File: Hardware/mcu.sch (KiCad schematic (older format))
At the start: 30 parts, among them J1 SWD_programming, U6 CY8C4246AZI-L445, Y1 Crystal

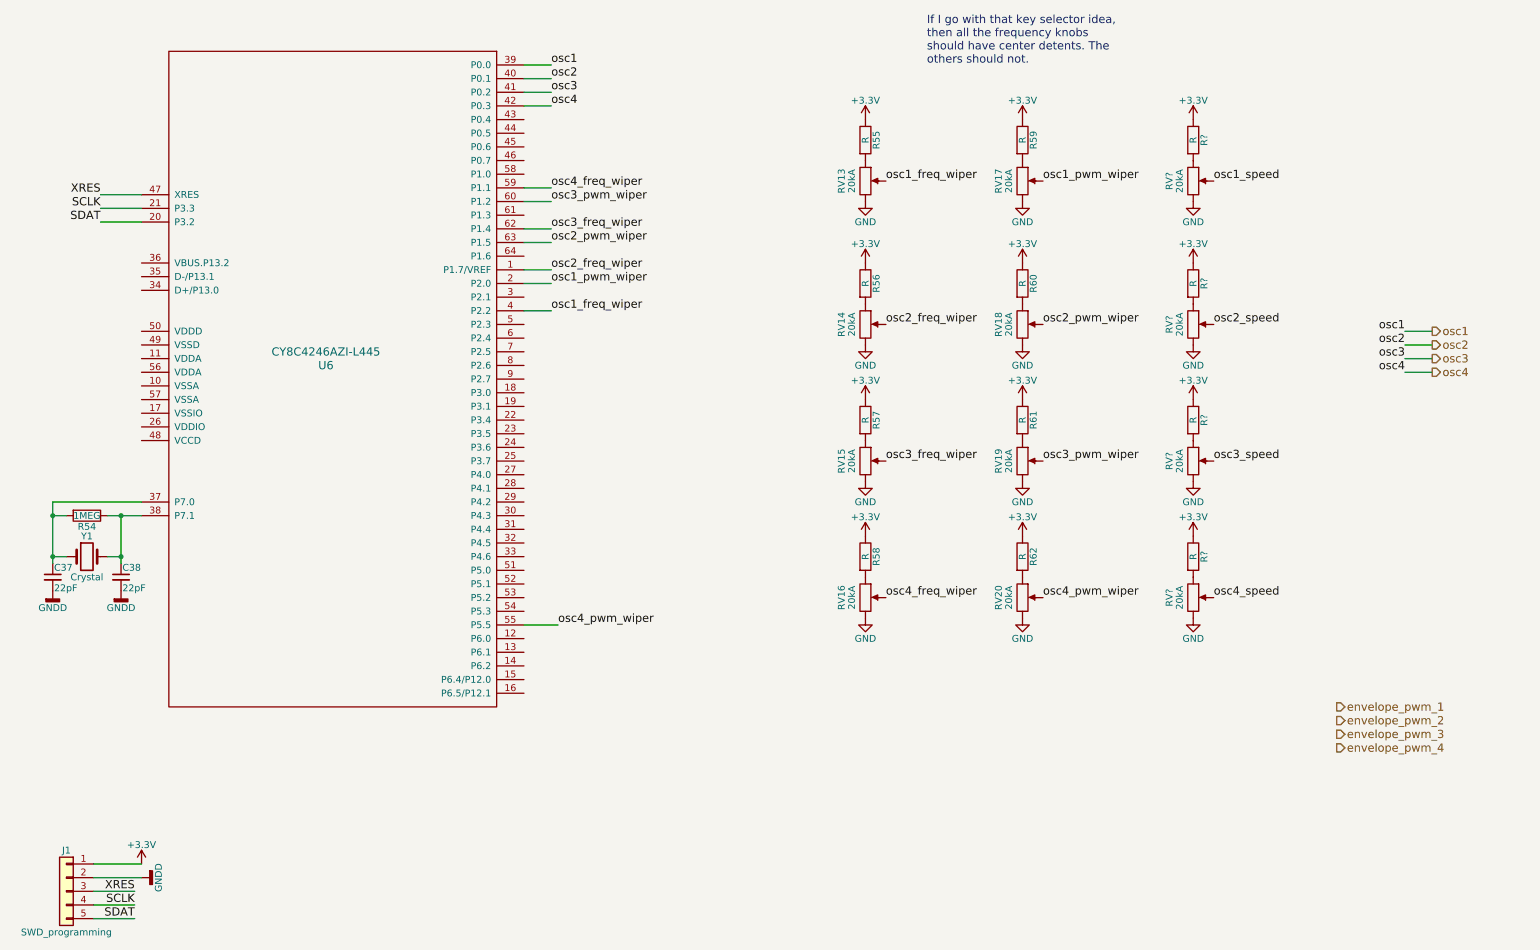
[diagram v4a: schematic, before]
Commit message: update pinout with latest changes for production IC
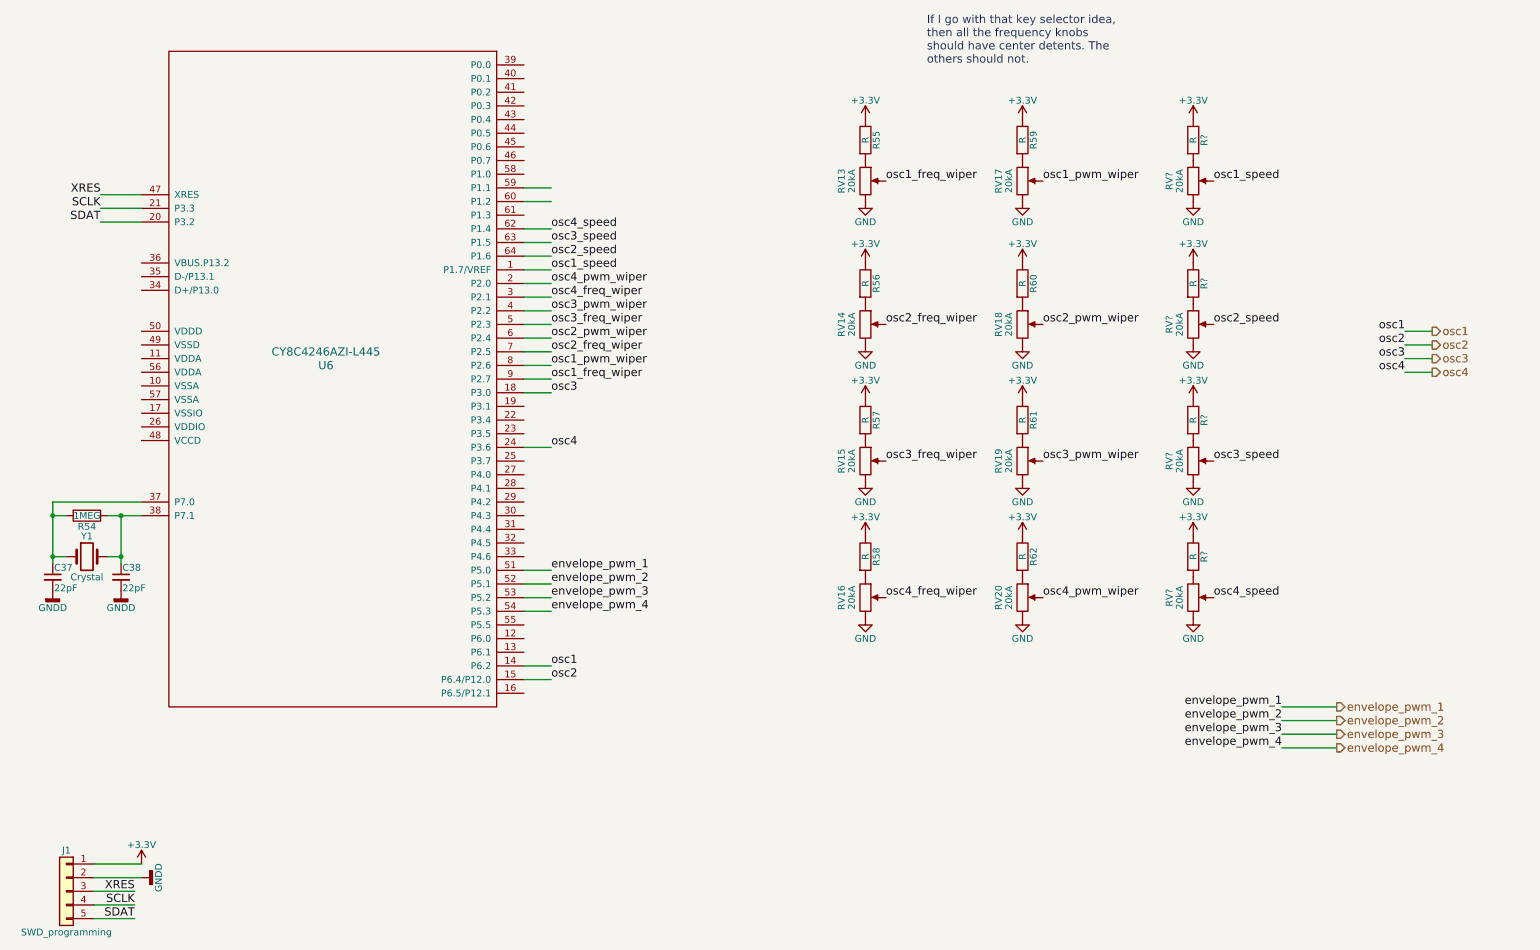
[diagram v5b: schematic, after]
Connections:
- wire segments 31 -> 45
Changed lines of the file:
@@
 	-1   0    0    -1
 $EndComp
+Text Label 4400 3400 0    60   ~ 0
+osc1_freq_wiper
+Wire Wire Line
+	4400 2900 4200 2900
+Text Label 4400 3300 0    60   ~ 0
+osc1_pwm_wiper
+Wire Wire Line
+	4400 2700 4200 2700
+Text Label 4400 3200 0    60   ~ 0
+osc2_freq_wiper
+Wire Wire Line
+	4400 2600 4200 2600
+Text Label 4400 3100 0    60   ~ 0
+osc2_pwm_wiper
+Wire Wire Line
+	4400 2400 4200 2400
+Text Label 4400 3000 0    60   ~ 0
+osc3_freq_wiper
+Wire Wire Line
+	4400 2300 4200 2300
 Text Label 4400 2900 0    60   ~ 0
-osc1_freq_wiper
-Wire Wire Line
-	4400 2900 4200 2900
+osc3_pwm_wiper
+Wire Wire Line
+	4400 2100 4200 2100
+Text Label 4400 2800 0    60   ~ 0
+osc4_freq_wiper
+Wire Wire Line
+	4400 2000 4200 2000
 Text Label 4400 2700 0    60   ~ 0
-osc1_pwm_wiper
-Wire Wire Line
-	4400 2700 4200 2700
-Text Label 4400 2600 0    60   ~ 0
-osc2_freq_wiper
-Wire Wire Line
-	4400 2600 4200 2600
-Text Label 4400 2400 0    60   ~ 0
-osc2_pwm_wiper
-Wire Wire Line
-	4400 2400 4200 2400
-Text Label 4400 2300 0    60   ~ 0
-osc3_freq_wiper
-Wire Wire Line
-	4400 2300 4200 2300
-Text Label 4400 2100 0    60   ~ 0
-osc3_pwm_wiper
-Wire Wire Line
-	4400 2100 4200 2100
-Text Label 4400 2000 0    60   ~ 0
-osc4_freq_wiper
-Wire Wire Line
-	4400 2000 4200 2000
-Text Label 4450 5200 0    60   ~ 0
 osc4_pwm_wiper
-Wire Wire Line
-	4450 5200 4200 5200
-Text Label 4400 1100 0    60   ~ 0
+Text Label 4400 5500 0    60   ~ 0
 osc1
-Text Label 4400 1200 0    60   ~ 0
+Text Label 4400 5600 0    60   ~ 0
 osc2
-Text Label 4400 1300 0    60   ~ 0
+Text Label 4400 3500 0    60   ~ 0
 osc3
-Text Label 4400 1400 0    60   ~ 0
+Text Label 4400 3900 0    60   ~ 0
 osc4
-Wire Wire Line
-	4400 1100 4200 1100
-Wire Wire Line
-	4400 1200 4200 1200
-Wire Wire Line
-	4200 1300 4400 1300
-Wire Wire Line
-	4400 1400 4200 1400
 Text Label 10650 3050 2    60   ~ 0
 osc1
@@
 	1    0    0    -1
 $EndComp
+Wire Wire Line
+	4400 3400 4200 3400
+Wire Wire Line
+	4400 3300 4200 3300
+Wire Wire Line
+	4400 3200 4200 3200
+Wire Wire Line
+	4400 3100 4200 3100
+Wire Wire Line
+	4400 3000 4200 3000
+Wire Wire Line
+	4400 2800 4200 2800
+Text Label 4400 2600 0    60   ~ 0
+osc1_speed
+Text Label 4400 2500 0    60   ~ 0
+osc2_speed
+Text Label 4400 2400 0    60   ~ 0
+osc3_speed
+Text Label 4400 2300 0    60   ~ 0
+osc4_speed
+Wire Wire Line
+	4400 2500 4200 2500
+Wire Wire Line
+	4400 3500 4200 3500
+Wire Wire Line
+	4400 3900 4200 3900
+Text Label 4400 4800 0    60   ~ 0
+envelope_pwm_1
+Wire Wire Line
+	4400 5500 4200 5500
+Wire Wire Line
+	4200 5600 4400 5600
+Wire Wire Line
+	4400 4800 4200 4800
+Text Label 4400 4900 0    60   ~ 0
+envelope_pwm_2
+Text Label 4400 5000 0    60   ~ 0
+envelope_pwm_3
+Text Label 4400 5100 0    60   ~ 0
+envelope_pwm_4
+Wire Wire Line
+	4400 4900 4200 4900
+Wire Wire Line
+	4200 5000 4400 5000
+Wire Wire Line
+	4200 5100 4400 5100
+Text Label 9750 5800 2    60   ~ 0
+envelope_pwm_1
+Wire Wire Line
+	9750 5800 10150 5800
+Text Label 9750 5900 2    60   ~ 0
+envelope_pwm_2
+Text Label 9750 6000 2    60   ~ 0
+envelope_pwm_3
+Text Label 9750 6100 2    60   ~ 0
+envelope_pwm_4
+Wire Wire Line
+	9750 5900 10150 5900
+Wire Wire Line
+	9750 6000 10150 6000
+Wire Wire Line
+	9750 6100 10150 6100
 $EndSCHEMATC

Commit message: associate footprints with all components
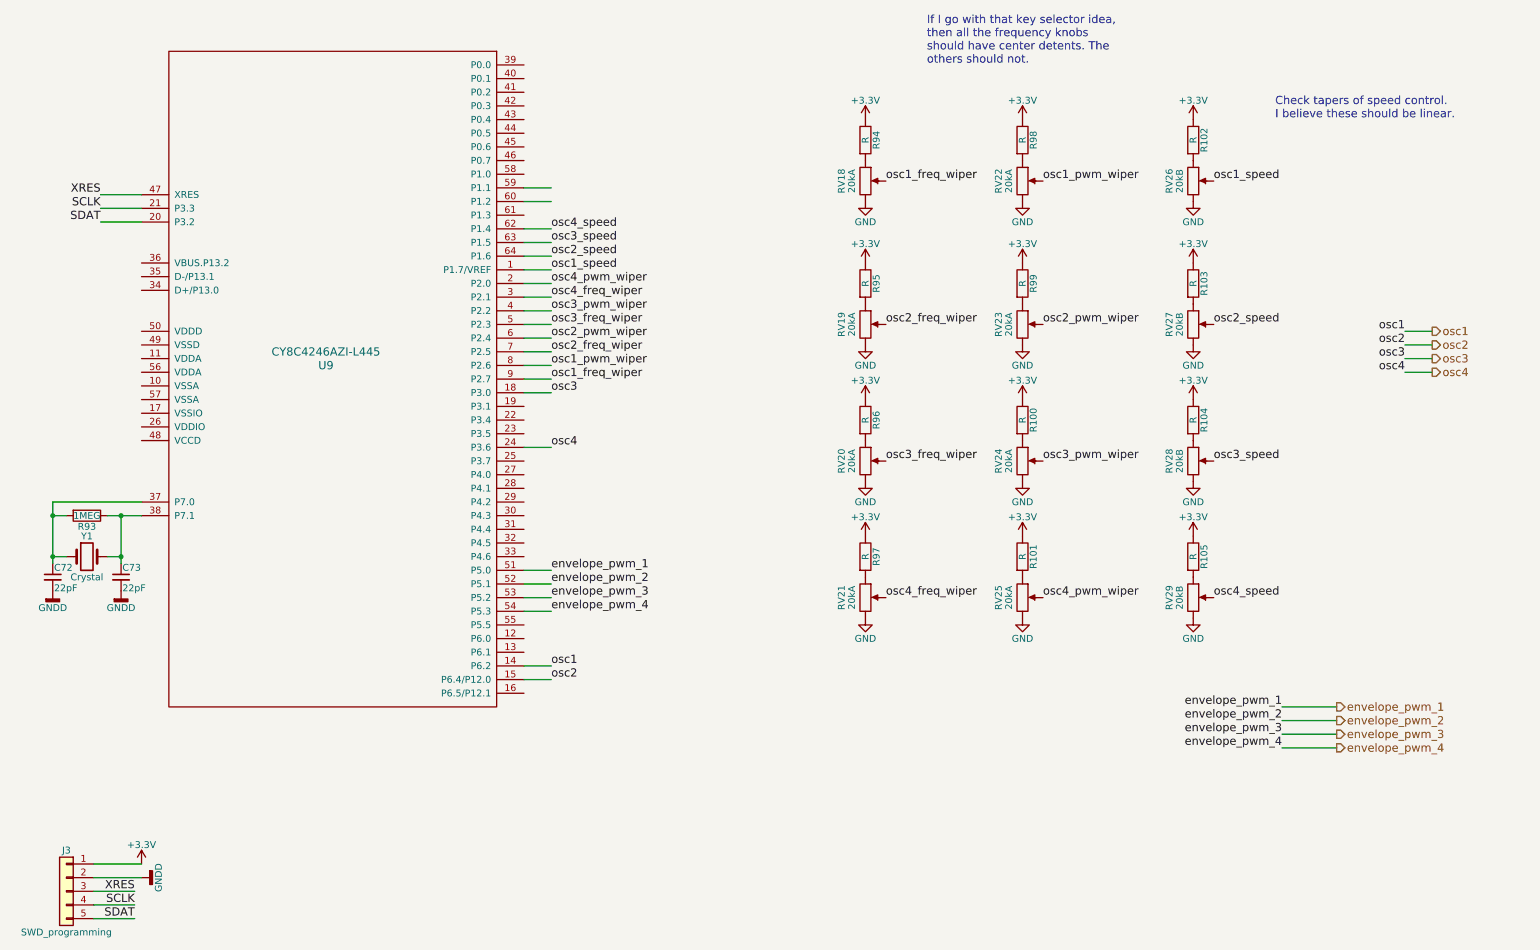
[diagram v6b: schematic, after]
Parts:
- C72: renamed from C37; footprint (none) -> digikey-footprints:0805
- C73: renamed from C38; footprint (none) -> digikey-footprints:0805
- J3: renamed from J1; footprint (none) -> Pin_Headers:Pin_Header_Straight_1x05_Pitch2.54mm
- R100: renamed from R61; footprint (none) -> digikey-footprints:0805
- R101: renamed from R62; footprint (none) -> digikey-footprints:0805
- R102, R103, R104, R105: renamed from R?; footprint (none) -> digikey-footprints:0805
- R93: renamed from R54; footprint (none) -> digikey-footprints:0805
- R94: renamed from R55; footprint (none) -> digikey-footprints:0805
- R95: renamed from R56; footprint (none) -> digikey-footprints:0805
- R96: renamed from R57; footprint (none) -> digikey-footprints:0805
- R97: renamed from R58; footprint (none) -> digikey-footprints:0805
- R98: renamed from R59; footprint (none) -> digikey-footprints:0805
- R99: renamed from R60; footprint (none) -> digikey-footprints:0805
- RV18: renamed from RV13; footprint (none) -> Potentiometers:Potentiometer_Bourns_PTV09A-1_Horizontal
- RV19: renamed from RV14; footprint (none) -> Potentiometers:Potentiometer_Bourns_PTV09A-1_Horizontal
- RV20: renamed from RV15; footprint (none) -> Potentiometers:Potentiometer_Bourns_PTV09A-1_Horizontal
- RV21: renamed from RV16; footprint (none) -> Potentiometers:Potentiometer_Bourns_PTV09A-1_Horizontal
- RV22: renamed from RV17; footprint (none) -> Potentiometers:Potentiometer_Bourns_PTV09A-1_Horizontal
- RV23: renamed from RV18; footprint (none) -> Potentiometers:Potentiometer_Bourns_PTV09A-1_Horizontal
- RV24: renamed from RV19; footprint (none) -> Potentiometers:Potentiometer_Bourns_PTV09A-1_Horizontal
- RV25: renamed from RV20; footprint (none) -> Potentiometers:Potentiometer_Bourns_PTV09A-1_Horizontal
- RV26, RV27, RV28, RV29: renamed from RV?; value 20kA -> 20kB; footprint (none) -> Potentiometers:Potentiometer_Bourns_PTV09A-1_Horizontal
- U9: renamed from U6; footprint (none) -> digikey-footprints:LQFP-64_10x10mm
- Y1: footprint (none) -> Crystals:Crystal_SMD_HC49-SD_HandSoldering
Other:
- note added: "Check tapers of speed control.\nI believe these should be linear."

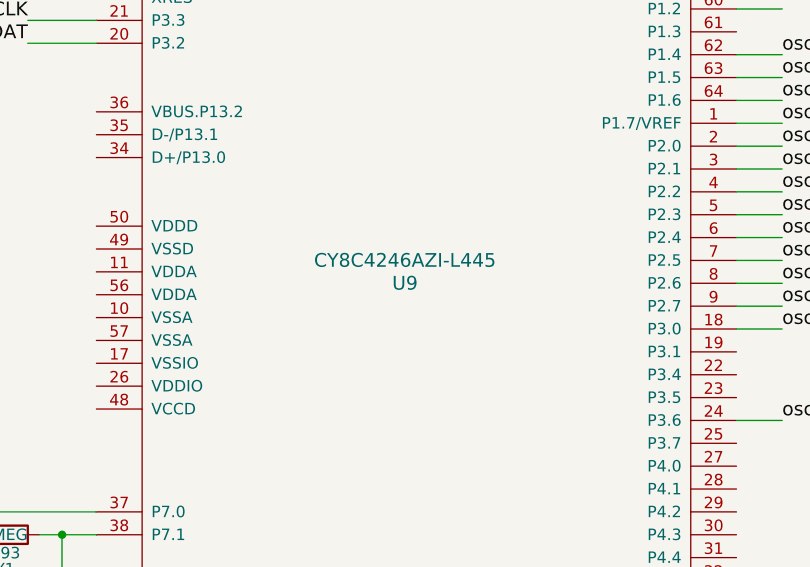
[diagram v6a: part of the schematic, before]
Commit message: fix annotation and footprints for multi-part op amps.
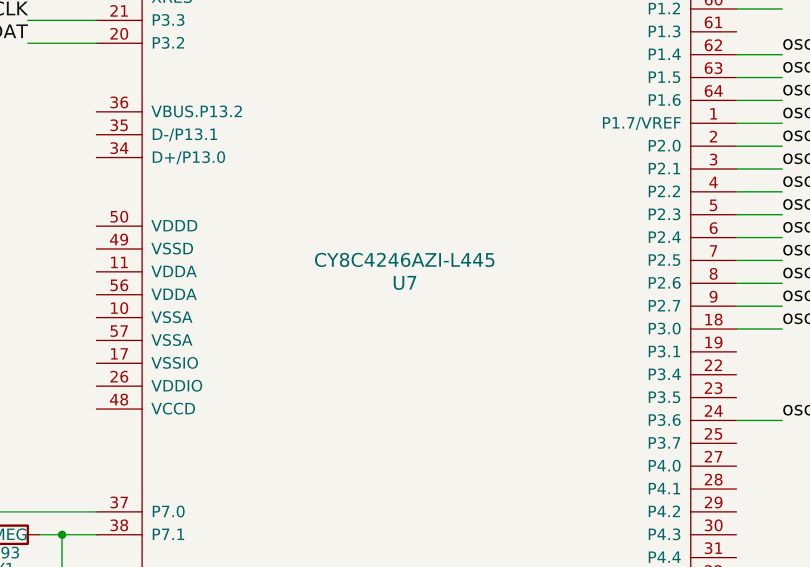
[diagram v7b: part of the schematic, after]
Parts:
- renumbered U9 to U7
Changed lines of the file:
@@
 Connection ~ 1250 4700
 $Comp
-L CY8C4246AZI-L445 U9
+L CY8C4246AZI-L445 U7
 U 1 1 5C36E7A3
 P 2800 3250
-F 0 "U9" H 2850 3200 60  0000 C CNN
+F 0 "U7" H 2850 3200 60  0000 C CNN
 F 1 "CY8C4246AZI-L445" H 2850 3300 60  0000 C CNN
 F 2 "digikey-footprints:LQFP-64_10x10mm" H 2900 3200 60  0001 C CNN

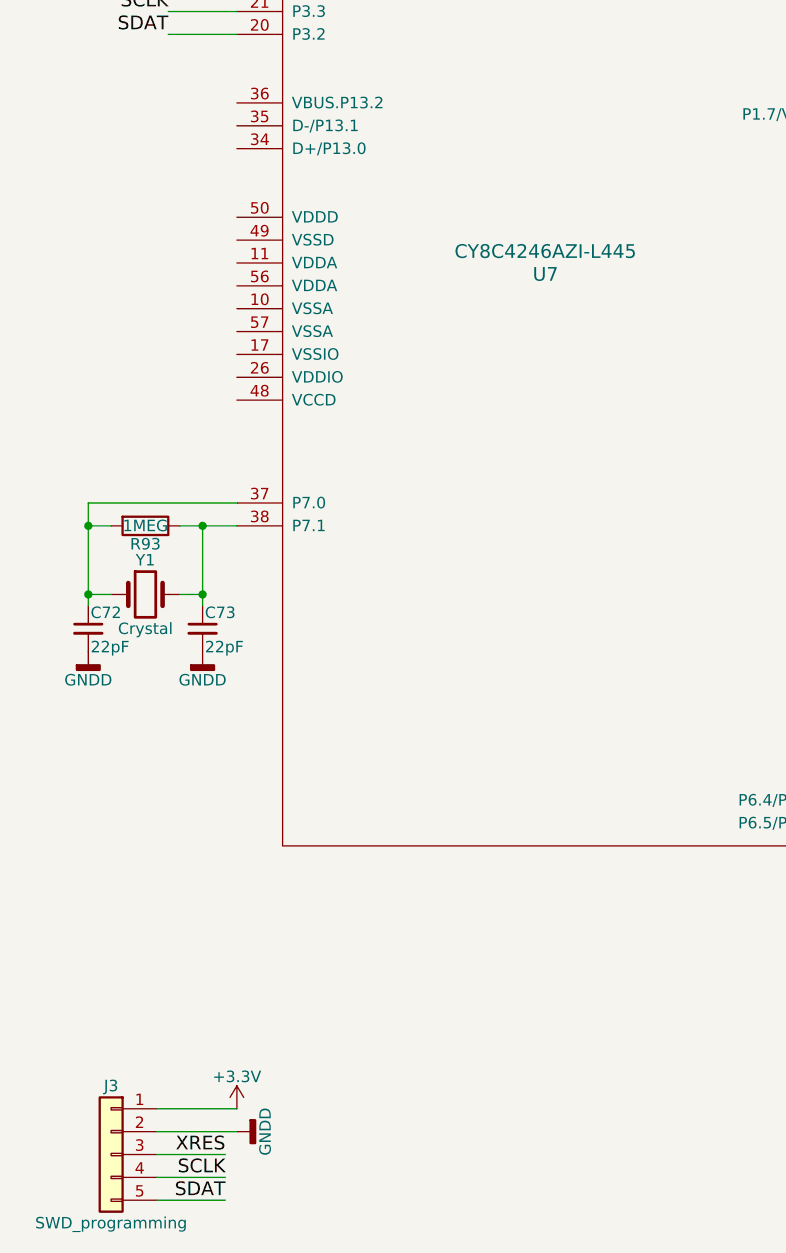
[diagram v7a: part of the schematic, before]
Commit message: loosely organize components into groups based on their functionality
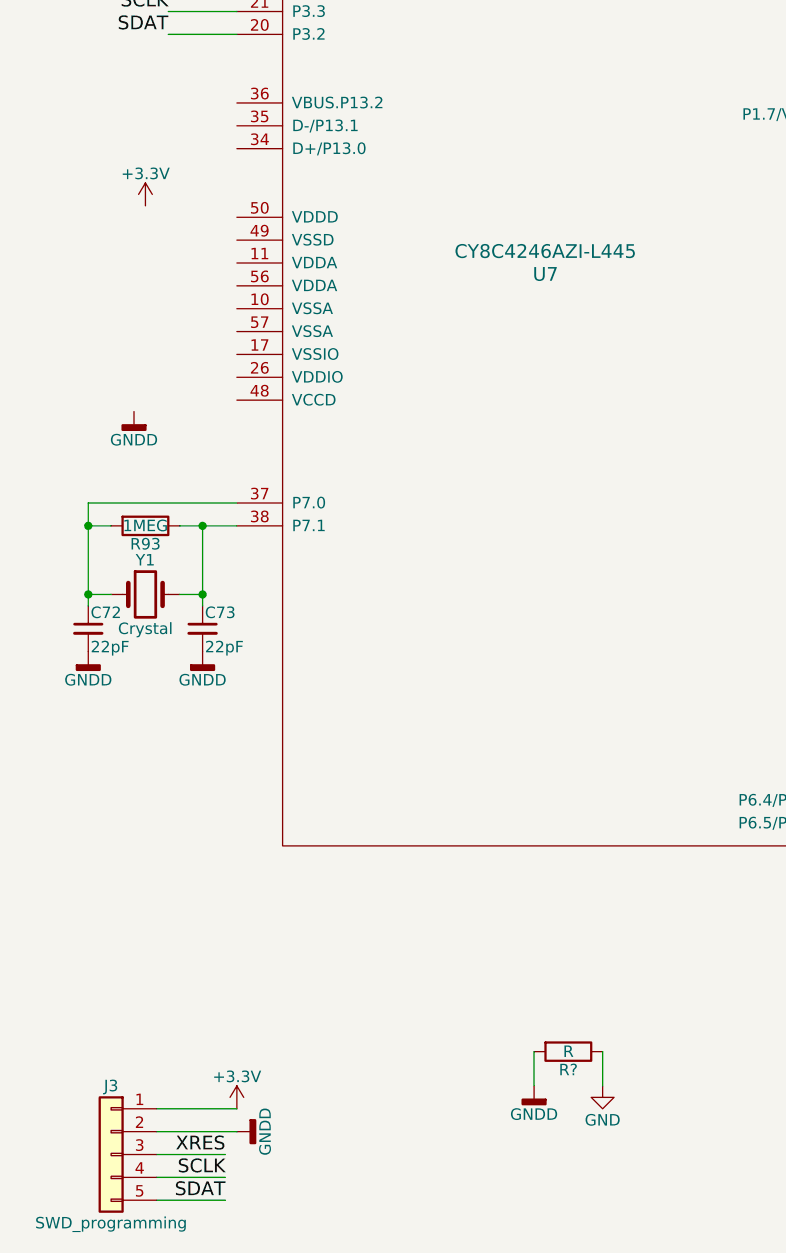
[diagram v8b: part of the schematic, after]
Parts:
- added R?: R, symbol R
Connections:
- wire segments 45 -> 47
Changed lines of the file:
@@
 Text Notes 9700 1500 0    60   ~ 0
 Check tapers of speed control.\nI believe these should be linear.
+$Comp
+L +3.3V #PWR?
+U 1 1 5C3F0EDD
+P 1000 3000
+F 0 "#PWR?" H 1000 2850 50  0001 C CNN
+F 1 "+3.3V" H 1000 3140 50  0000 C CNN
+F 2 "" H 1000 3000 50  0001 C CNN
+F 3 "" H 1000 3000 50  0001 C CNN
+	1    1000 3000
+	1    0    0    -1
+$EndComp
+$Comp
+L GNDD #PWR?
+U 1 1 5C3F1075
+P 950 3900
+F 0 "#PWR?" H 950 3650 50  0001 C CNN
+F 1 "GNDD" H 950 3775 50  0000 C CNN
+F 2 "" H 950 3900 50  0001 C CNN
+F 3 "" H 950 3900 50  0001 C CNN
+	1    950  3900
+	-1   0    0    -1
+$EndComp
+$Comp
+L GNDD #PWR?
+U 1 1 5C3F13C8
+P 2700 6850
+F 0 "#PWR?" H 2700 6600 50  0001 C CNN
+F 1 "GNDD" H 2700 6725 50  0000 C CNN
+F 2 "" H 2700 6850 50  0001 C CNN
+F 3 "" H 2700 6850 50  0001 C CNN
+	1    2700 6850
+	-1   0    0    -1
+$EndComp
+$Comp
+L GND #PWR?
+U 1 1 5C3F1411
+P 3000 6850
+F 0 "#PWR?" H 3000 6600 50  0001 C CNN
+F 1 "GND" H 3000 6700 50  0000 C CNN
+F 2 "" H 3000 6850 50  0001 C CNN
+F 3 "" H 3000 6850 50  0001 C CNN
+	1    3000 6850
+	1    0    0    -1
+$EndComp
+$Comp
+L R R?
+U 1 1 5C3F1461
+P 2850 6700
+F 0 "R?" V 2930 6700 50  0000 C CNN
+F 1 "R" V 2850 6700 50  0000 C CNN
+F 2 "" V 2780 6700 50  0001 C CNN
+F 3 "" H 2850 6700 50  0001 C CNN
+	1    2850 6700
+	0    1    1    0
+$EndComp
+Wire Wire Line
+	2700 6700 2700 6850
+Wire Wire Line
+	3000 6700 3000 6850
 $EndSCHEMATC
